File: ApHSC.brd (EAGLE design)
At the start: 35 x 35 mm, 24 parts, among them U1 ATMEGA328P-AU, U2 UA78M05, U3 TPL7407L, U4 A2982

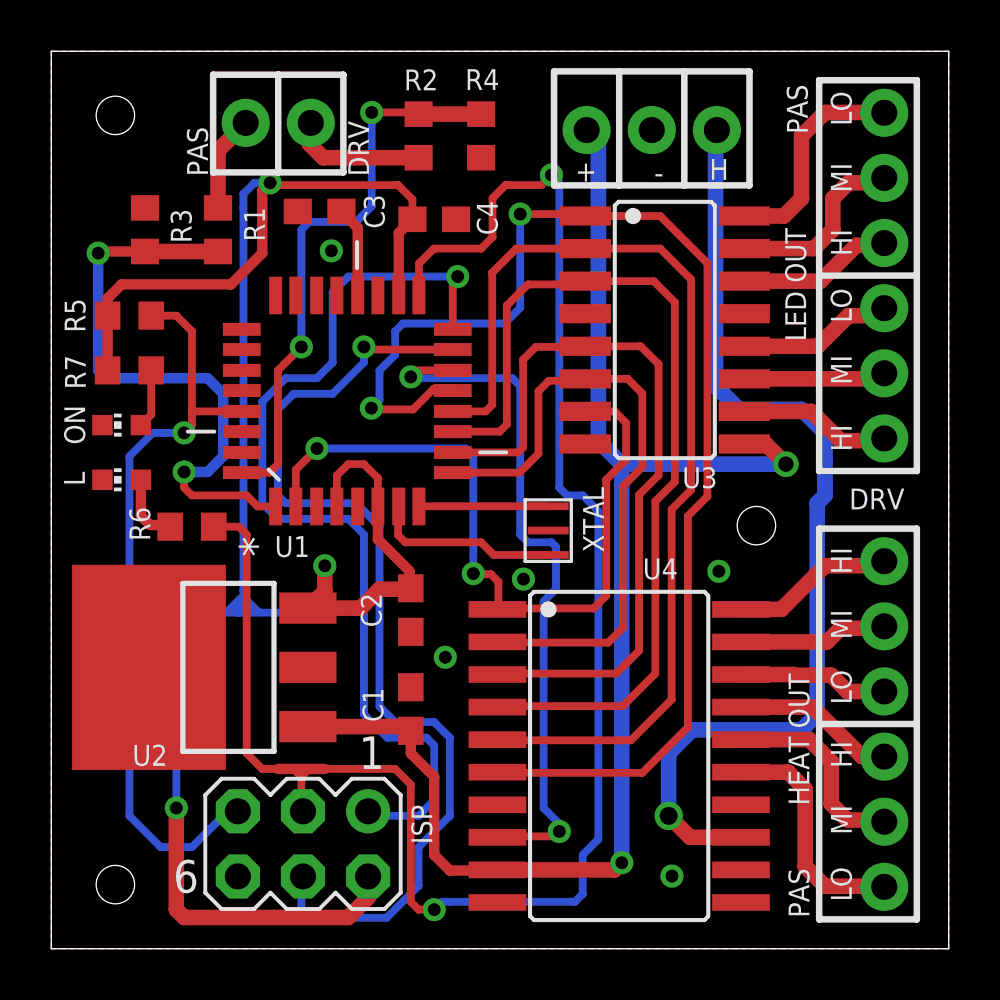
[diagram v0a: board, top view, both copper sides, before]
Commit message: Small layout changes - tweaked position of vias and silkscreen.
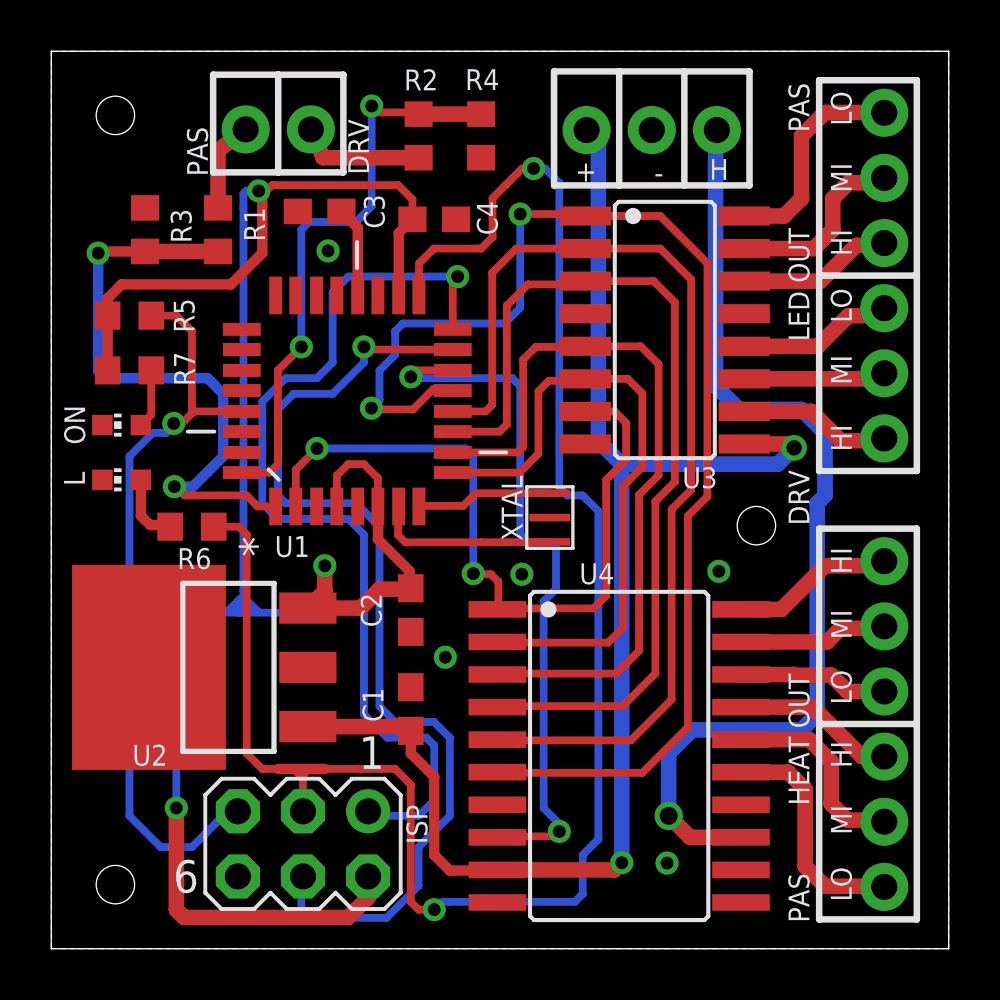
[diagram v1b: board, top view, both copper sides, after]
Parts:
- moved XTAL 0.51 mm to (19.4, 16.8)
- moved BTN-IN 0.25 mm to (7.58, 32.0)
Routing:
- net VIN: track 54.5 -> 55.1 mm
